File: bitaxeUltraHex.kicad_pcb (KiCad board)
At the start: 4 copper layers, 84.5 x 129.5 mm, 333 parts, among them J1 Conn_01x01, J2 Conn_01x01, J3 TC2030-IDC, J4 USB_C_Receptacle_USB2.0, J5 Conn_01x04, J6 Conn_01x04, Q1 NTMFS5C673NLT1G, Q2 CSD17577Q5A, Q3 NTMFS5C673NLT1G, Q4 CSD17577Q5A, Q5 BSS123, SW1 GT-TC029B-H025-L1N, SW2 GT-TC029B-H025-L1N, U1 uA7805, U10 TMP1075, U11 TMP1075, U12 EMC2302, U13 BM1366_mode1, U14 ADP171AUJ-R7, U15 ADP171AUJ-R7, U16 BM1366_mode1, U17 25MHz, U18 TLV3544, U19 BM1366_mode0, U2 RT9080-33GJ5, U20 ADP171AUJ-R7, U21 ADP171AUJ-R7, U22 BM1366_mode0, U23 TLV3544, U24 BM1366_mode1, U25 ADP171AUJ-R7, U26 ADP171AUJ-R7, U27 BM1366_mode1, U3 INA219AIDCNR, U4 TPS40305, U5 MIC5504, U6 DS4432U+, U7 SN74AVC4T774, U8 176x320_st7789, U9 ESP32-S3-WROOM-1, Y1 32.768kHz

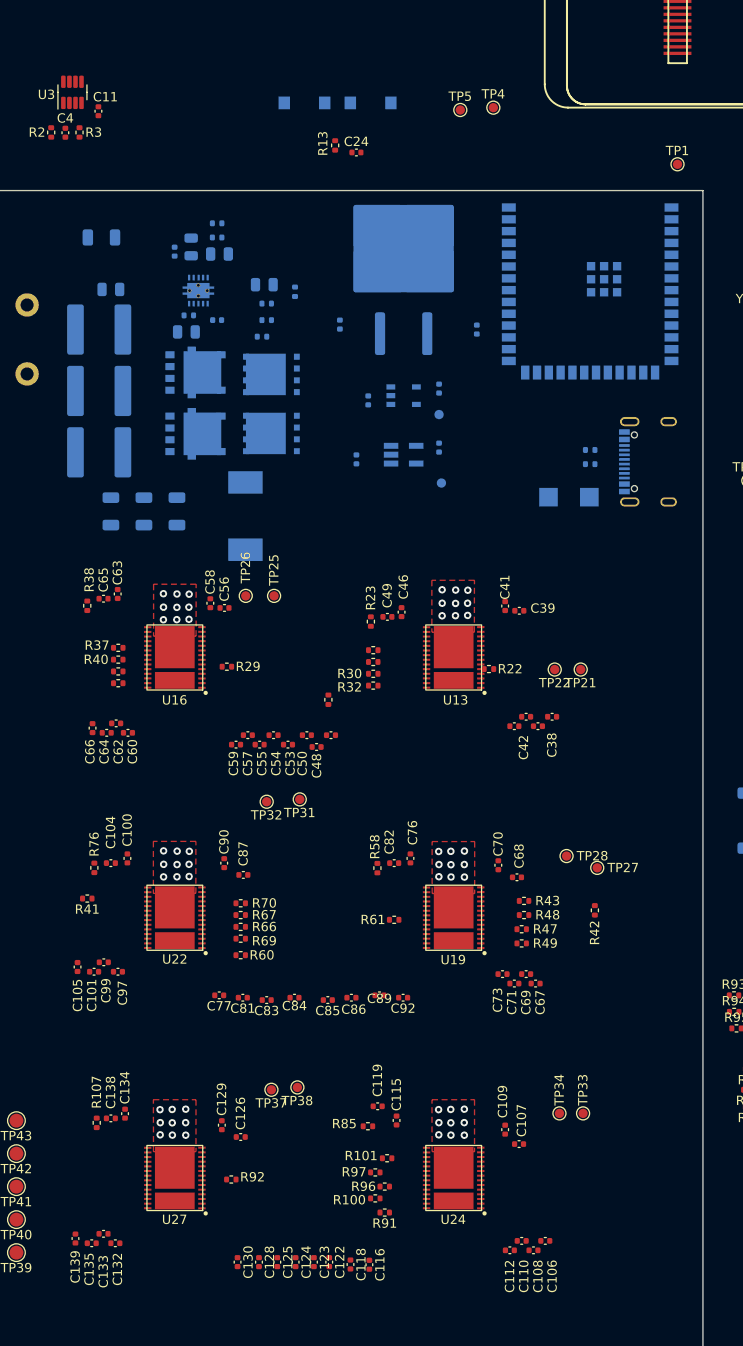
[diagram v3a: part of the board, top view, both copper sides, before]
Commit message: add some power planes and do some comms routing
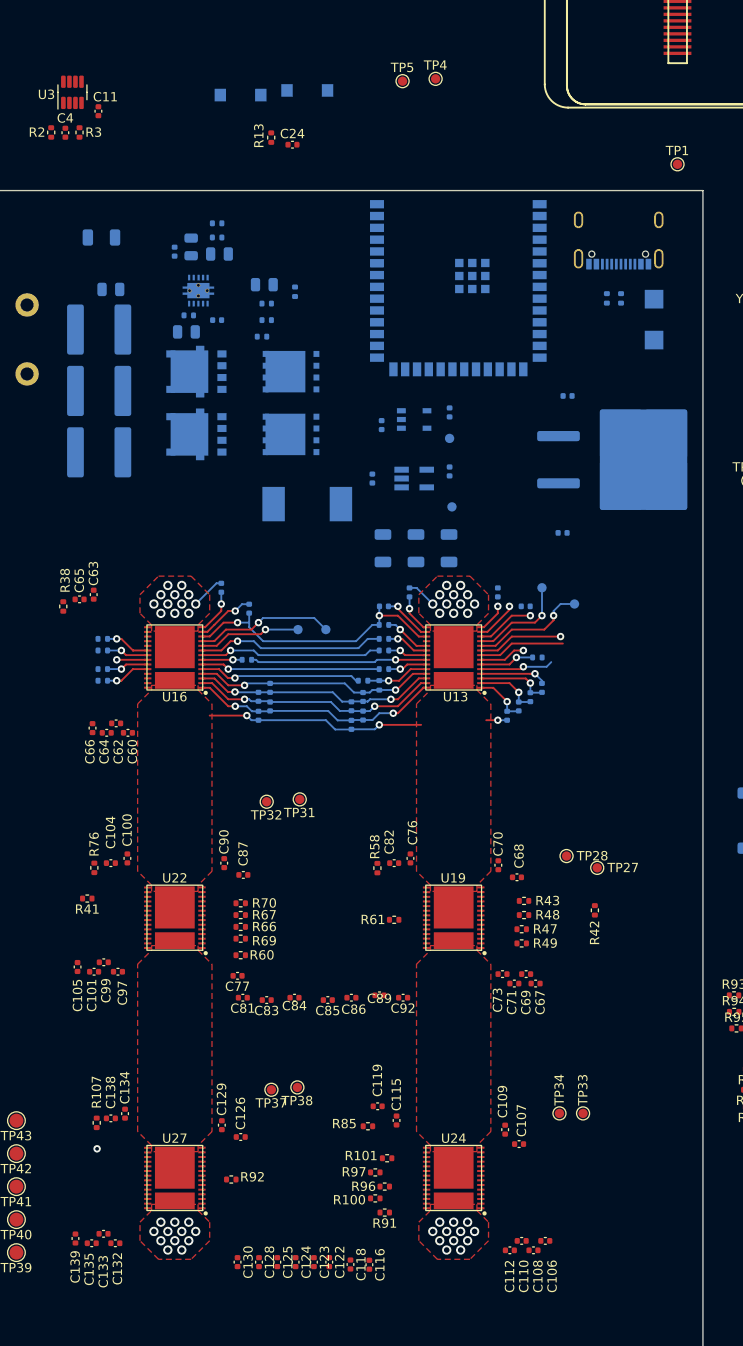
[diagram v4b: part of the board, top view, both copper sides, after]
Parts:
- C38, C39, C40, C41, C42, C43, C46, C47, C48, C49, C50, C53, C54, C55, C56, C57, C58, C59, R22, R23, R26, R29, R30, R31, R32, R33, R36, R37, R39, R40, TP21, TP22, TP25, TP26: moved to B.Cu
- moved C22 36.6 mm to (107.5, 85.2), turned to -90 degrees
- moved U1 32.3 mm to (126.9, 75.7), turned to 0 degrees
- moved C21 29.5 mm to (103.9, 85.2), turned to -90 degrees
- moved C12 25.7 mm to (120.3, 68.9), turned to 180 degrees
- moved J4 25.3 mm to (125.8, 51.0), turned to 0 degrees
- moved C3 23.7 mm to (119.7, 83.6), turned to 0 degrees
- moved C20 22.5 mm to (100.4, 85.2), turned to -90 degrees
- moved D1 21.2 mm to (129.6, 60.7), turned to 90 degrees
- moved R19 18.1 mm to (126.0, 58.4), turned to 90 degrees
- moved R18 16.4 mm to (124.5, 58.4), turned to 90 degrees
- moved U9 14.2 mm to (108.5, 56.5)
- moved C53 9.57 mm to (98.2, 101.2), turned to 90 degrees
- moved TP26 9.35 mm to (94.2, 94.0), turned to 0 degrees
- moved TP22 8.90 mm to (117.5, 89.5), turned to 0 degrees
- moved TP21 7.08 mm to (121.0, 91.2), turned to 0 degrees
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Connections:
- U17 pad 3: /BM1366-1/CLKI -> /BM1366-1/CLKI1
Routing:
- net Net-(U13-MODE_1): track 0.00 -> 30.6 mm, vias 0 -> 2
- net Net-(U13-VDD1_1): track 0.00 -> 27.1 mm, vias 0 -> 2
- net Net-(U13-VDD2_1): track 0.00 -> 26.7 mm, vias 0 -> 2
- net Net-(U13-VDD3_1): track 0.00 -> 26.3 mm, vias 0 -> 2
- net Net-(C53-Pad2): track 0.00 -> 26.0 mm, vias 0 -> 2
- net /BM1366-1/VDD1: track 0.00 -> 25.8 mm, vias 18 -> 3
- net Net-(U16-CI): track 0.00 -> 20.2 mm, vias 0 -> 1
- net Net-(U16-CLKI): track 0.00 -> 19.7 mm, vias 0 -> 1
- net Net-(U16-BI): track 0.00 -> 19.3 mm, vias 0 -> 1
- net Net-(U13-RI): track 0.00 -> 19.0 mm, vias 0 -> 1
- net Net-(U16-NRSTI): track 0.00 -> 17.5 mm, vias 0 -> 1
- net /BM1366-1/0V8: track 0.00 -> 16.4 mm, vias 0 -> 3
- net /BM1366-1/TEMP_N2_1: track 0.00 -> 14.9 mm, vias 0 -> 1
- net /BM1366-1/TEMP_P1_1: track 0.00 -> 12.5 mm, vias 0 -> 1
- net /BM1366-1/1V2: track 0.00 -> 12.2 mm, vias 0 -> 3
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- added copper zone on In2.Cu, net /BM1366-1/VDD1
- added copper zone on In2.Cu, net /BM1366-2/VDD2
- added copper zone on F.Cu, net /VDD
- added copper zone on In1.Cu, net /VDD
- added copper zone on In2.Cu, net GND
- removed copper zone on In2.Cu, net /3V3
- removed copper zone on In1.Cu, net /BM1366-1/VDD1
- removed copper zone on In1.Cu, net /BM1366-2/VDD2
- removed copper zone on In1.Cu, net GND

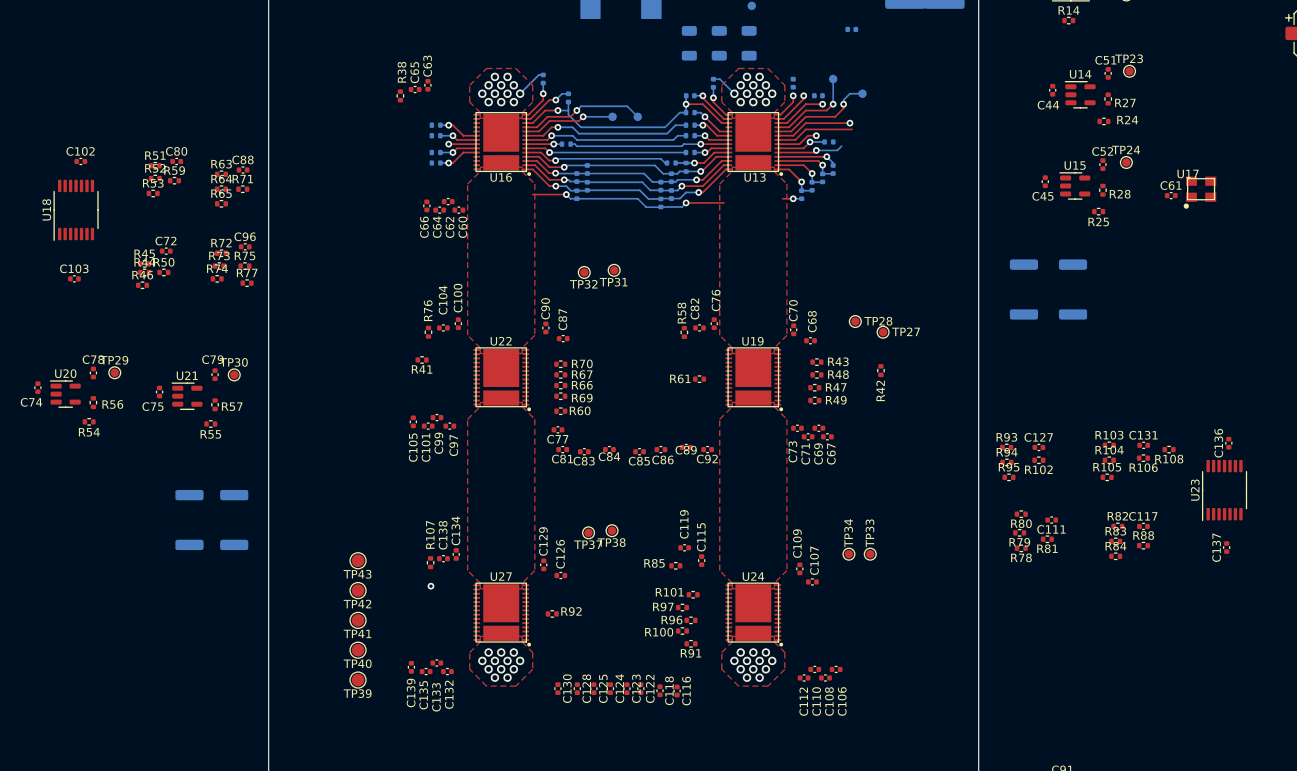
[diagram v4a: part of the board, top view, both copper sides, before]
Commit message: Arrange the comms voltage level translators
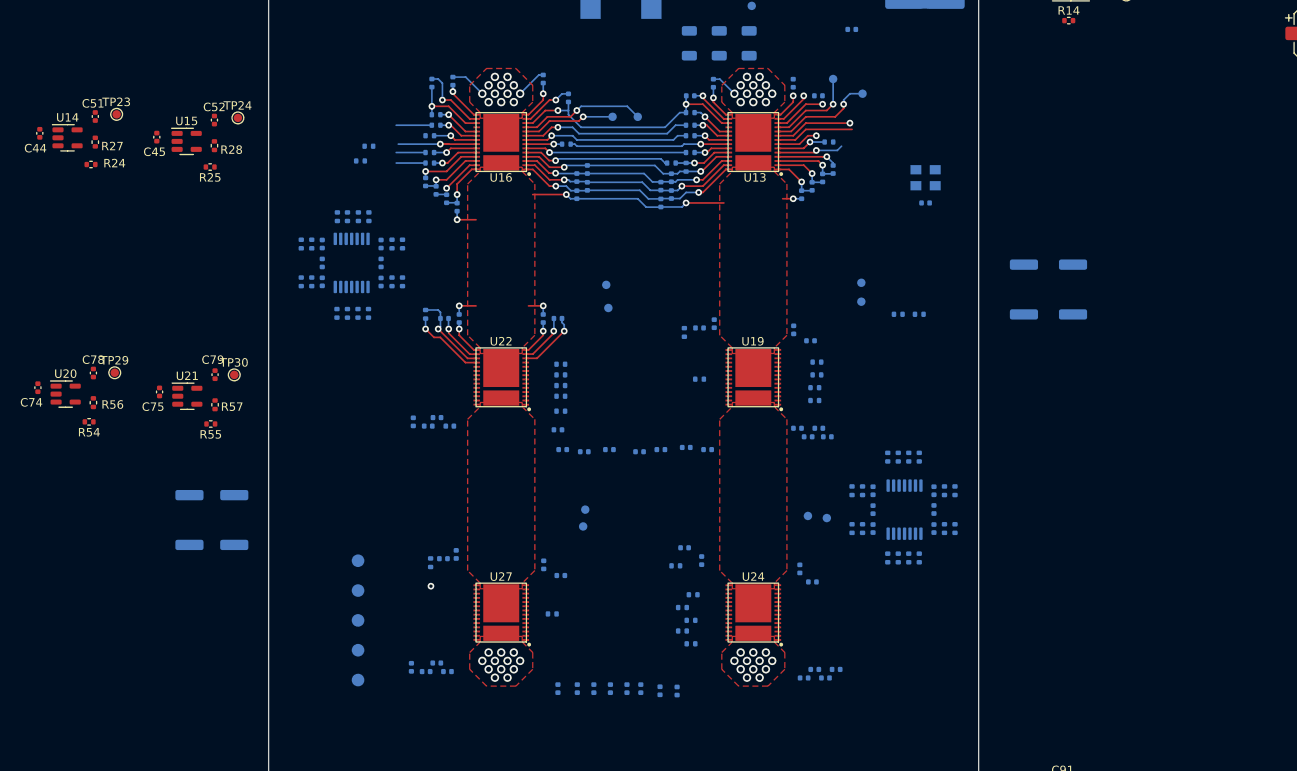
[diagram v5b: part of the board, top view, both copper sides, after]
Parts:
- C100, C101, C102, C103, C104, C105, C106, C107, C108, C109, C110, C111, C112, C115, C116, C117, C118, C119, C122, C123, C124, C125, C126, C127, C128, C129, C130, C131, C132, C133, C134, C135, C136, C137, C138, C139, C60, C61, C62, C63, C64, C65, C66, C67, C68, C69, C70, C71, C72, C73, C76, C77, C80, C81, C82, C83, C84, C85, C86, C87, C88, C89, C90, C92, C96, C97, C99, R100, R101, R102, R103, R104, R105, R106, R107, R108, R38, R41, R42, R43, R44, R45, R46, R47, R48, R49, R50, R51, R52, R53, R58, R59, R60, R61, R63, R64, R65, R66, R67, R69, R70, R71, R72, R73, R74, R75, R76, R77, R78, R79, R80, R81, R82, R83, R84, R85, R88, R91, R92, R93, R94, R95, R96, R97, TP27, TP28, TP31, TP32, TP33, TP34, TP37, TP38, TP39, TP40, TP41, TP42, TP43, U17, U18, U23: moved to B.Cu
- moved C51 120.7 mm to (29.7, 94.0)
- moved R27 120.7 mm to (29.7, 97.0)
- moved U14 120.7 mm to (26.4, 96.5)
- moved C44 120.7 mm to (23.1, 96.0)
- moved R24 120.7 mm to (29.2, 99.7)
- moved TP23 120.7 mm to (32.2, 93.7)
- moved R25 105.9 mm to (43.4, 100.0)
- moved TP24 105.9 mm to (46.7, 94.1)
- moved U15 105.9 mm to (40.6, 96.9)
- moved C52 105.9 mm to (43.9, 94.4)
- moved R28 105.9 mm to (43.9, 97.4)
- moved C45 105.9 mm to (37.0, 96.4)
- moved C137 42.3 mm to (122.2, 140.8), turned to -90 degrees
- moved U23 38.2 mm to (126.0, 140.8)
- moved C102 37.7 mm to (63.7, 111.4), turned to -90 degrees
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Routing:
- net /BM1366-2/0V8: track 0.00 -> 12.3 mm, vias 0 -> 2
- net Net-(U22-MODE_1): track 0.00 -> 10.0 mm, vias 0 -> 1
- net Net-(U16-MODE_1): track 0.00 -> 9.46 mm, vias 0 -> 1
- net /BM1366-1/VDD1: track 25.8 -> 34.9 mm, vias 3 -> 6
- net Net-(U22-MODE_0): track 0.00 -> 8.98 mm, vias 0 -> 1
- net /BM1366-2/1V2: track 0.00 -> 8.65 mm, vias 0 -> 2
- net /BM1366-1/0V8: track 16.4 -> 24.9 mm, vias 3 -> 4
- net Net-(U16-VDD3_1): track 0.00 -> 7.80 mm, vias 0 -> 1
- net Net-(C66-Pad2): track 0.00 -> 7.58 mm, vias 0 -> 1
- net Net-(U19-MODE_1): track 0.00 -> 7.54 mm, vias 0 -> 1
- net Net-(U16-RI): track 3.33 -> 10.3 mm
- net Net-(U16-VDD1_1): track 0.00 -> 6.60 mm, vias 0 -> 1
- net Net-(U16-VDD2_1): track 0.00 -> 5.99 mm, vias 0 -> 1
- net Net-(U16-NC): track 0.00 -> 5.15 mm, vias 0 -> 1
- net /BM1366-1/1V2: track 12.2 -> 17.1 mm, vias 3 -> 4
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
